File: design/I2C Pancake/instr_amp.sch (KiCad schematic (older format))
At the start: 9 parts, among them U1 INA826

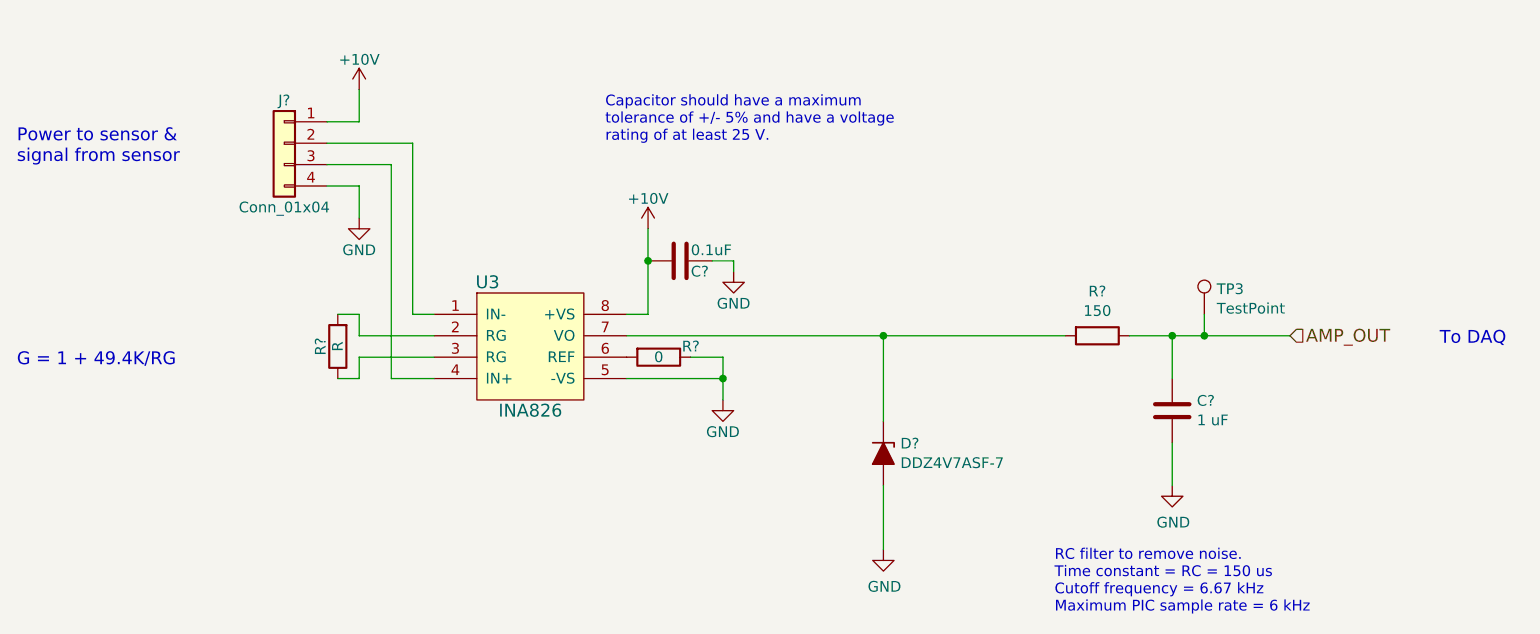
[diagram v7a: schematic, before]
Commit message: Repair broken and missing library references
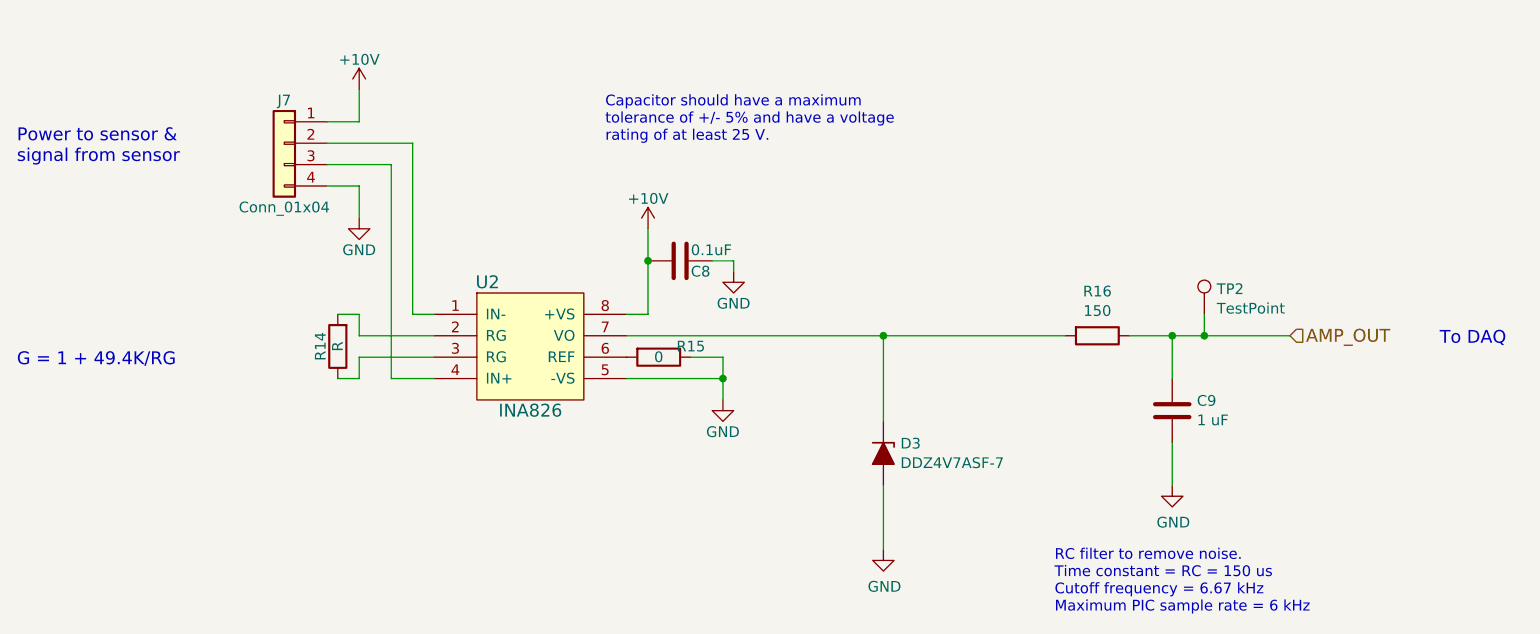
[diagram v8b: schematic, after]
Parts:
- gave numbers to parts that had none: 7
